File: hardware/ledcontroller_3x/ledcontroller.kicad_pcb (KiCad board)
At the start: 4 copper layers, 35.6 x 59.1 mm, 88 parts, among them J1 ADC, J10 GPIO10, J11 MOSI, J12 SCLK, J13 TX, J14 RX, J15 FLASH, J16 SCL, J17 SDA, J18 OE, J19 Pololu D24V5F3, J2 GPIO16, J20 VIN, J21 GND, J22 24V, J23 RED, J24 GREEN, J25 BLUE, J26 W_WHITE, J27 C_WHITE, J28 24V, J29 RED, J3 GPIO14, J30 GREEN, J31 BLUE, J32 W_WHITE, J33 C_WHITE, J34 24V, J35 RED, J36 GREEN, J37 BLUE, J38 W_WHITE, J39 C_WHITE, J4 GPIO12, J5 GPIO13, J6 RESET, J7 CS0, J8 MISO, J9 GPIO9, Q1 BLM3400, Q10 BLM3400, Q11 BLM3400, Q12 BLM3400, Q13 BLM3400, Q14 BLM3400, Q15 BLM3400, Q2 BLM3400, Q3 BLM3400, Q4 BLM3400, Q5 BLM3400, Q6 BLM3400, Q7 BLM3400, Q8 BLM3400, Q9 BLM3400, U1 ESP-12E, U2 PCA9685PW

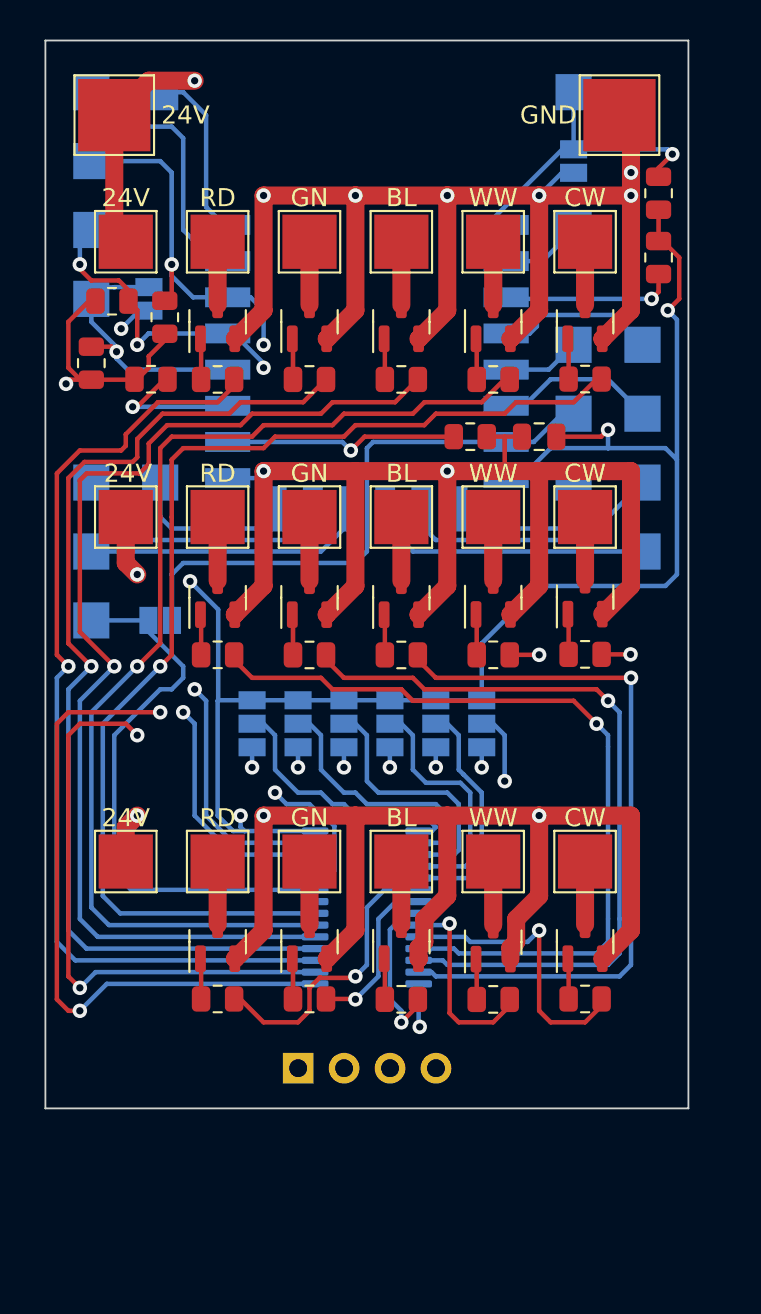
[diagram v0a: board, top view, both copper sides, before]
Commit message: Updated PCB to combat flickering with higher current LEDs or longer strips
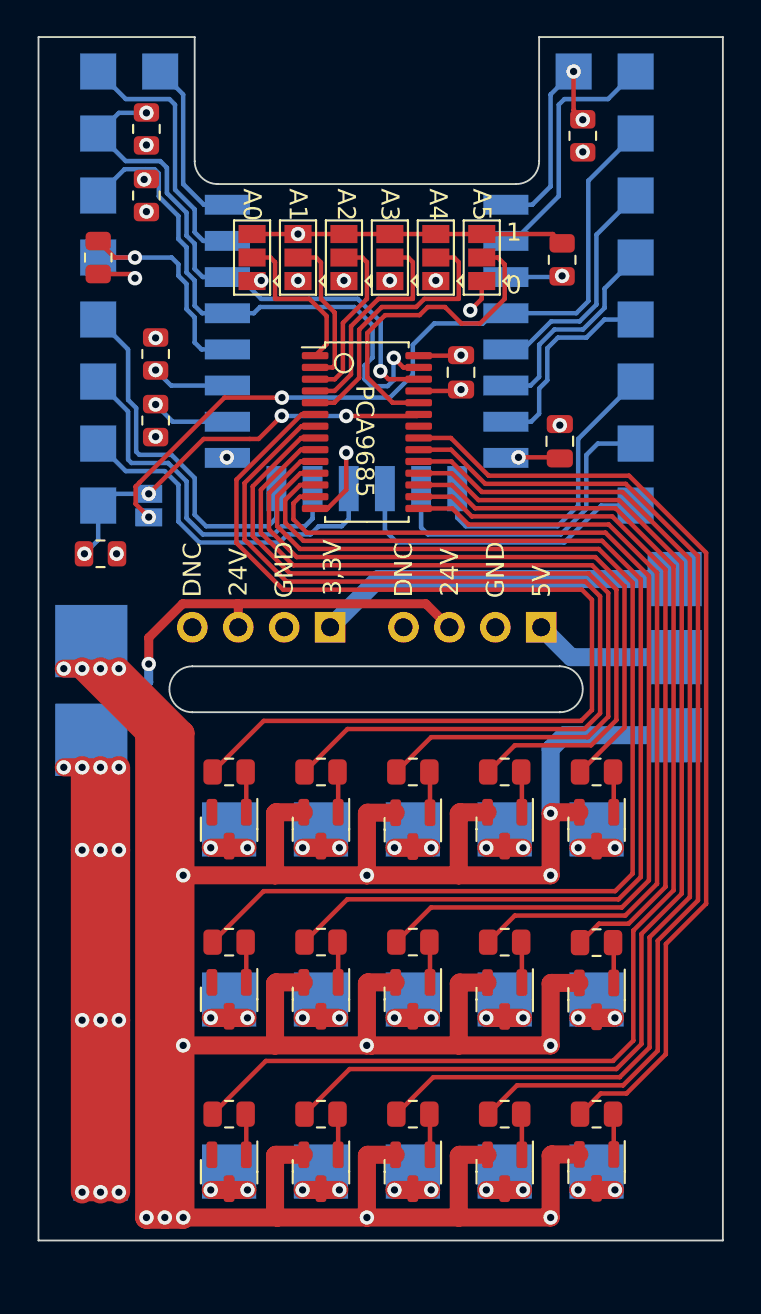
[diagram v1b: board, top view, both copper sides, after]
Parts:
- removed JP8: RESET, Jumper:SolderJumper-2_P1.3mm_Open_Pad1.0x1.5mm
- removed JP9: FLASH, Jumper:SolderJumper-2_P1.3mm_Open_Pad1.0x1.5mm
- added C2: 100nF, Capacitor_SMD:C_0805_2012Metric, F.Cu at (114.8, 68.8)
- added J40: Pololu D24V5F5, Connector_PinHeader_2.54mm:PinHeader_1x04_P2.54mm_Vertical, B.Cu at (113.8, 79.1)
- added J41: AUX, TestPoint:TestPoint_Pad_3.0x3.0mm, B.Cu at (121.2, 80.8)
- added J43: GND, TestPoint:TestPoint_Pad_3.0x3.0mm, B.Cu at (121.2, 85.1)
- added J45: 3.3V, TestPoint:TestPoint_Pad_3.0x3.0mm, B.Cu at (121.2, 76.5)
- added R23: 10k, Resistor_SMD:R_0805_2012Metric, F.Cu at (89.4, 75.1)
- J20, J21, J22, J23, J24, J25, J26, J27, J28, J29, J30, J31, J32, J33, J34, J35, J36, J37, J38, J39: moved to B.Cu
- JP1, JP2, JP3, JP4, JP5, JP7, U2: moved to F.Cu
- moved J22 51.6 mm to (89.4, 109.3), turned to 180 degrees
- moved J23 51.4 mm to (96.5, 109.2), turned to 180 degrees
- moved J24 51.4 mm to (101.6, 109.2), turned to 180 degrees
- moved J25 51.4 mm to (106.7, 109.2), turned to 180 degrees
- moved J26 51.4 mm to (111.8, 109.2), turned to 180 degrees
- moved J27 51.4 mm to (116.8, 109.2), turned to 180 degrees
- moved Q1 47.0 mm to (96.5, 109.2), turned to -90 degrees
- moved Q2 47.0 mm to (101.6, 109.2), turned to -90 degrees
- moved Q3 47.0 mm to (106.7, 109.2), turned to -90 degrees
- moved Q4 47.0 mm to (111.8, 109.2), turned to -90 degrees
- moved Q5 47.0 mm to (116.8, 109.2), turned to -90 degrees
- moved J21 41.2 mm to (88.9, 79.9), turned to 180 degrees
- moved R12 40.7 mm to (116.8, 106.0), turned to 0 degrees
- moved R10 40.6 mm to (106.7, 106.0), turned to 0 degrees
- moved R11 40.6 mm to (111.8, 106.0), turned to 0 degrees
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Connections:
- net Net-(R3-Pad2) renamed /RST
- net Net-(R5-Pad2) renamed /FLS
- net Net-(U1-Pad17) renamed /CS0
- net Net-(U1-Pad18) renamed /MISO
- net Net-(U1-Pad19) renamed /G9
- net Net-(U1-Pad2) renamed /ADC
- net Net-(U1-Pad20) renamed /G10
- net Net-(U1-Pad21) renamed /MOSI
- net Net-(U1-Pad22) renamed /SCLK
- net Net-(U1-Pad5) renamed /G14
- net Net-(U1-Pad6) renamed /G12
- net Net-(U2-Pad1) renamed /A0
- net Net-(U2-Pad2) renamed /A1
- net Net-(U2-Pad23) renamed /OE
- net Net-(U2-Pad24) renamed /A5
- net Net-(U2-Pad3) renamed /A2
- net Net-(U2-Pad4) renamed /A3
- net Net-(U2-Pad5) renamed /A4
- J2 pad 1: Net-(U1-Pad4) -> /G16
- J5 pad 1: Net-(U1-Pad7) -> /G13
- JP6 pad 1: Net-(U1-Pad7) -> /G16
- U1 pad 4: Net-(U1-Pad4) -> /G16
- U1 pad 7: Net-(U1-Pad7) -> /G13
- U2 pad 25: unconnected-(U2-Pad25) -> GND
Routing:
- net +24V: track 18.7 -> 105.8 mm, vias 3 -> 14
- net +3.3V: track 129.1 -> 44.3 mm, vias 5 -> 9
- net /Green0: track 9.23 -> 53.5 mm, vias 1 -> 0
- net /G16: track 0.00 -> 42.6 mm, vias 0 -> 2
- net /Red0: track 16.4 -> 58.8 mm, vias 1 -> 0
- net /Blue0: track 9.00 -> 48.1 mm, vias 1 -> 0
- net Net-(U1-Pad7): track 31.8 -> 0.00 mm
- net /WW0: track 11.0 -> 42.8 mm, vias 1 -> 0
- net GND: track 213.3 -> 241.3 mm, vias 18 -> 27
- net /SCL: track 57.3 -> 30.5 mm, vias 3 -> 2
- net /CW1: track 65.4 -> 38.9 mm, vias 3 -> 0
- net /CW0: track 16.0 -> 37.5 mm, vias 1 -> 0
- net /Red1: track 45.0 -> 66.1 mm, vias 1 -> 0
- net /SDA: track 51.2 -> 31.2 mm, vias 4 -> 2
- net /WW1: track 61.9 -> 42.5 mm, vias 3 -> 0
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- added copper zone on In1.Cu, net +24V
- added copper zone on In1.Cu, net +3.3V
- added copper zone on In2.Cu, net GND
- removed copper zone on In2.Cu, net +24V
- removed copper zone on In1.Cu, net GND
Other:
- board size 35.6 x 59.1 mm -> 37.8 x 66.5 mm
- board text added: "0"
- board text added: "1"
- board text added: "3,3V"
- board text added: "3.3V"
- board text added: "5V"
- board text added: "CH1"
- board text added: "CH2"
- board text added: "CH3"
- board text added: "CS"
- board text added: "DNC"
- board text added: "G9"
- board text added: "INPUT"
- board text added: "OE-G16"
- board text added: "OUTPUT"
- board text removed: "CS0"
- board text removed: "DNC,24V,GND,3.3V"
- board text removed: "G09"

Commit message: Updated PCB: additional decoupling capacitors, switchable I2C pullups, made OE pulled down instead of pulled up
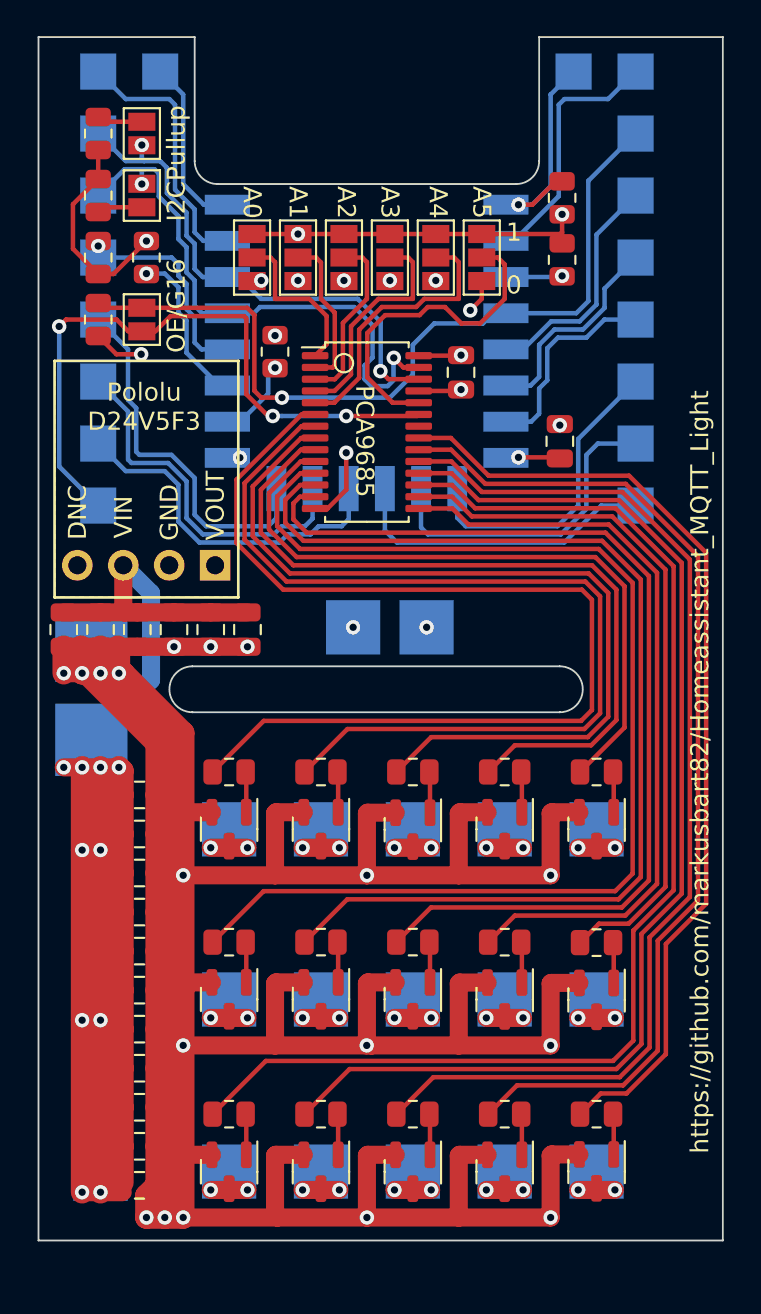
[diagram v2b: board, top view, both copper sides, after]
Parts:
- removed J40: Pololu D24V5F5, Connector_PinHeader_2.54mm:PinHeader_1x04_P2.54mm_Vertical
- removed J41: AUX, TestPoint:TestPoint_Pad_3.0x3.0mm
- added C10: 10uF 50V, Capacitor_SMD:C_0805_2012Metric, F.Cu at (91.6, 94.9)
- added C11: 10uF 50V, Capacitor_SMD:C_0805_2012Metric, F.Cu at (91.6, 92.7)
- added C12: 10uF 50V, Capacitor_SMD:C_0805_2012Metric, F.Cu at (91.6, 90.6)
- added C13: 10uF 50V, Capacitor_SMD:C_0805_2012Metric, F.Cu at (91.6, 88.4)
- added C14: 10uF 50V, Capacitor_SMD:C_0805_2012Metric, F.Cu at (87.4, 79.2)
- added C15: 10uF 50V, Capacitor_SMD:C_0805_2012Metric, F.Cu at (89.4, 79.2)
- added C16: 10uF 50V, Capacitor_SMD:C_0805_2012Metric, F.Cu at (91.4, 79.2)
- added C17: 10uF 50V, Capacitor_SMD:C_0805_2012Metric, F.Cu at (93.5, 79.2)
- added C18: 10uF 50V, Capacitor_SMD:C_0805_2012Metric, F.Cu at (95.5, 79.2)
- added C19: 10uF 50V, Capacitor_SMD:C_0805_2012Metric, F.Cu at (97.5, 79.2)
- added C3: 10uF 50V, Capacitor_SMD:C_0805_2012Metric, F.Cu at (91.6, 110.0)
- added C4: 10uF 50V, Capacitor_SMD:C_0805_2012Metric, F.Cu at (91.6, 107.8)
- added C5: 10uF 50V, Capacitor_SMD:C_0805_2012Metric, F.Cu at (91.6, 105.7)
- added C6: 10uF 50V, Capacitor_SMD:C_0805_2012Metric, F.Cu at (91.6, 103.5)
- added C7: 10uF 50V, Capacitor_SMD:C_0805_2012Metric, F.Cu at (91.6, 101.3)
- added C8: 10uF 50V, Capacitor_SMD:C_0805_2012Metric, F.Cu at (91.6, 99.2)
- added C9: 10uF 50V, Capacitor_SMD:C_0805_2012Metric, F.Cu at (91.6, 97.0)
- added JP8: OE, Jumper:SolderJumper-2_P1.3mm_Open_Pad1.0x1.5mm, F.Cu at (91.7, 51.8)
- added JP9: OE, Jumper:SolderJumper-2_P1.3mm_Open_Pad1.0x1.5mm, F.Cu at (91.7, 55.2)
- JP6: moved to F.Cu
- moved J45 18.0 mm to (103.4, 79.1)
- moved J43 15.0 mm to (107.4, 79.1)
- moved R23 13.0 mm to (89.3, 62.1), turned to 90 degrees
- moved JP6 10.3 mm to (91.7, 62.1), turned to -90 degrees
- moved R7 7.62 mm to (99.1, 63.9), turned to -90 degrees
- moved J19 7.23 mm to (95.7, 75.7)
- moved R6 5.36 mm to (91.9, 58.7)
- moved R3 3.61 mm to (114.9, 55.4)
- moved R1 2.68 mm to (89.3, 51.8)
- moved R2 2.67 mm to (89.3, 55.2), turned to -90 degrees
- moved J21 0.25 mm to (88.9, 80.1)
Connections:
- R1 pad 2: /SCL -> Net-(R1-Pad2)
- R2 pad 2: /SDA -> Net-(R2-Pad2)
- R23 pad 1: /OE -> GND
- R23 pad 2: +3.3V -> /G16
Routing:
- net GND: track 241.3 -> 256.8 mm, vias 27 -> 31
- net /OE: track 22.8 -> 36.2 mm, vias 4 -> 3
- net +3.3V: track 44.3 -> 34.9 mm, vias 9 -> 6
- net +5V: track 8.06 -> 0.00 mm
- net Net-(R6-Pad1): track 5.02 -> 9.60 mm
- net +24V: track 105.8 -> 101.8 mm, vias 14 -> 10
- net /G16: track 42.6 -> 45.3 mm, vias 2 -> 1
- net Net-(R2-Pad2): track 0.00 -> 2.52 mm
- net Net-(R1-Pad2): track 0.00 -> 2.52 mm
- net /FLS: track 14.4 -> 12.0 mm
- net /SCL: track 30.5 -> 28.3 mm
- net Net-(R7-Pad2): track 5.06 -> 3.78 mm
- net /RST: track 13.3 -> 13.4 mm, vias 2 -> 1
- added copper zone on F.Cu, net GND
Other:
- board text added: "I2CPullup"
- board text added: "IN"
- board text added: "OE/G16"
- board text added: "OUT"
- board text added: "Pololu D24V5F3"
- board text added: "VIN"
- board text added: "VOUT"
- board text added: "https://github.com/markusbart82/Homeassistant_MQTT_Light"
- board text removed: "3,3V"
- board text removed: "5V"
- board text removed: "INPUT"
- board text removed: "OE-G16"
- board text removed: "OUTPUT"

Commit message: replaced ceramic capacitors with low ESR electrolytic caps
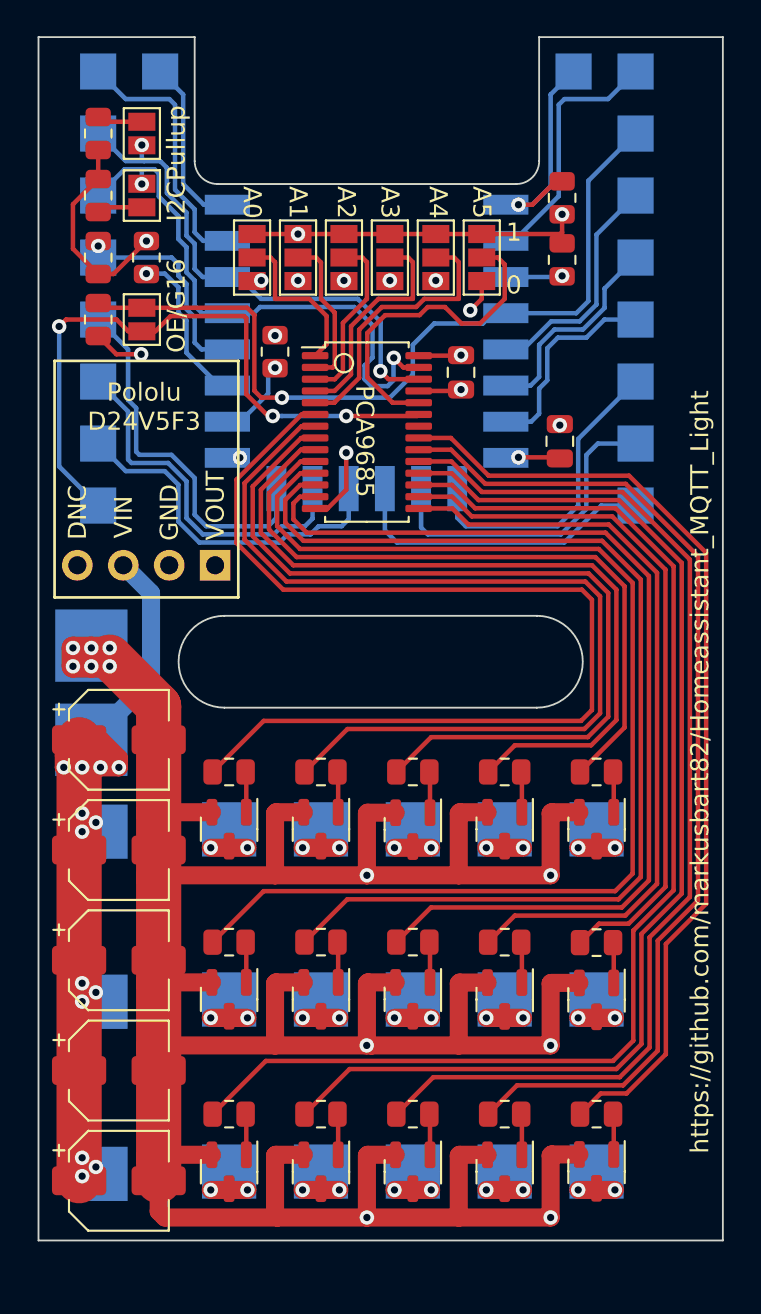
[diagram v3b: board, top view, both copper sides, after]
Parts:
- removed C10, C11, C12, C13, C14, C15, C16, C17, C18, C19, C8, C9: 10uF 50V, Capacitor_SMD:C_0805_2012Metric
- removed J43: GND, TestPoint:TestPoint_Pad_3.0x3.0mm
- removed J45: 3.3V, TestPoint:TestPoint_Pad_3.0x3.0mm
- C3, C4, C5, C6, C7: value 10uF 50V -> 10uF; footprint Capacitor_SMD:C_0805_2012Metric -> Capacitor_SMD:CP_Elec_5x5.4
- moved C3 24.7 mm to (90.4, 85.3)
- moved C4 16.4 mm to (90.4, 91.4)
- moved C7 8.46 mm to (90.4, 109.7)
- moved C5 8.21 mm to (90.4, 97.5)
- moved C6 1.15 mm to (90.4, 103.6)
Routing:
- net GND: track 256.8 -> 184.0 mm, vias 31 -> 24
- net +24V: track 101.8 -> 47.7 mm, vias 10 -> 13
- net +3.3V: vias 6 -> 5
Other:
- outline, holes or cut-outs redrawn
- board text removed: "3.3V"
- board text removed: "OUT"

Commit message: Added PCB Edge Connector for programming, rearranged lots of parts, removed pads of unused GPIOs
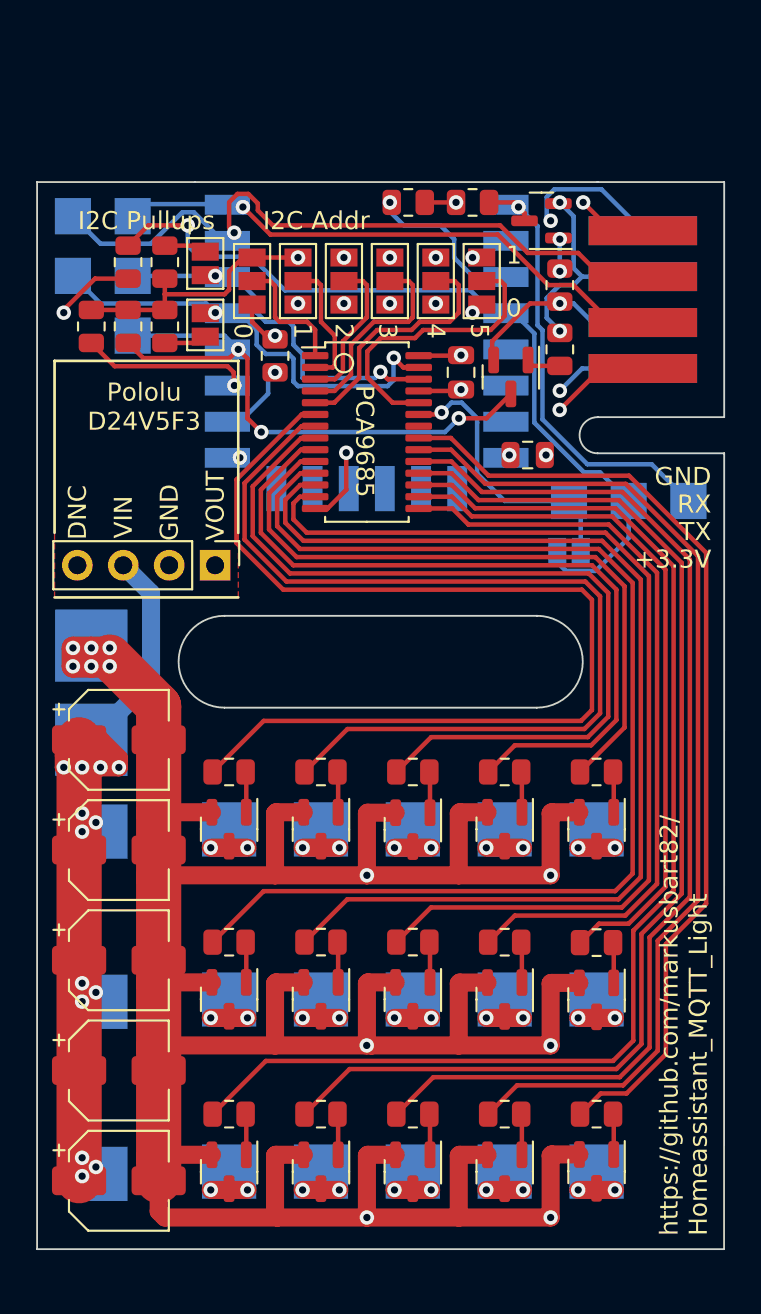
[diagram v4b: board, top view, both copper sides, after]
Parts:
- removed J1: ADC, TestPoint:TestPoint_Pad_2.0x2.0mm
- removed J10: GPIO10, TestPoint:TestPoint_Pad_2.0x2.0mm
- removed J11: MOSI, TestPoint:TestPoint_Pad_2.0x2.0mm
- removed J12: SCLK, TestPoint:TestPoint_Pad_2.0x2.0mm
- removed J3: GPIO14, TestPoint:TestPoint_Pad_2.0x2.0mm
- removed J4: GPIO12, TestPoint:TestPoint_Pad_2.0x2.0mm
- removed J5: GPIO13, TestPoint:TestPoint_Pad_2.0x2.0mm
- removed J7: CS0, TestPoint:TestPoint_Pad_2.0x2.0mm
- removed J8: MISO, TestPoint:TestPoint_Pad_2.0x2.0mm
- removed J9: GPIO9, TestPoint:TestPoint_Pad_2.0x2.0mm
- added J41: Flash Adapter, Connector_Card_Edge:WingTAT_ED08BGFBK, F.Cu at (121.9, 61.0)
- added Q16: MMS9013-H-TP, Package_TO_SOT_SMD:SOT-23, F.Cu at (113.8, 56.6)
- added Q17: MMS9013-H-TP, Package_TO_SOT_SMD:SOT-23, F.Cu at (112.1, 65.3)
- added R24: 10k, Resistor_SMD:R_0805_2012Metric, F.Cu at (114.8, 60.2)
- added R25: 10k, Resistor_SMD:R_0805_2012Metric, F.Cu at (114.8, 63.8)
- C3, C4, C5, C6, C7: value 10uF -> 10uF 35V
- J19: moved to F.Cu
- JP6: moved to B.Cu
- moved JP6 26.9 mm to (115.3, 74.9), turned to 0 degrees
- moved J18 26.0 mm to (115.3, 72.1)
- moved J6 24.6 mm to (121.9, 72.1)
- moved J2 20.3 mm to (118.6, 72.1)
- moved R4 9.08 mm to (106.4, 55.6), turned to 180 degrees
- moved J13 8.14 mm to (91.2, 56.4)
- moved R2 8.12 mm to (93.0, 62.5)
- moved J14 8.12 mm to (87.9, 56.4)
- moved J16 8.10 mm to (91.2, 59.7)
- moved R1 8.01 mm to (93.0, 58.9)
- moved JP8 7.99 mm to (95.2, 59.0)
- moved JP9 7.97 mm to (95.2, 62.4)
- moved R3 4.96 mm to (110.0, 55.6), turned to 0 degrees
- moved R6 4.88 mm to (88.9, 62.5)
- moved J15 4.72 mm to (91.2, 63.0)
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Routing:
- net /RX: track 15.2 -> 38.8 mm, vias 0 -> 1
- net /TX: track 10.4 -> 31.8 mm, vias 0 -> 1
- net /SCLK: track 21.3 -> 0.00 mm
- net /MOSI: track 20.8 -> 0.00 mm
- net /FLS: track 12.0 -> 32.6 mm, vias 1 -> 3
- net /OE: track 36.2 -> 15.7 mm, vias 3 -> 1
- net /G10: track 20.2 -> 0.00 mm
- net /MISO: track 18.7 -> 0.00 mm
- net /G9: track 18.0 -> 0.00 mm
- net /CS0: track 17.8 -> 0.00 mm
- net /ADC: track 14.7 -> 0.00 mm
- net /G14: track 13.7 -> 0.00 mm
- net /RTS: track 0.00 -> 12.5 mm, vias 0 -> 2
- net /G12: track 12.5 -> 0.00 mm
- net /G13: track 12.1 -> 0.00 mm
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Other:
- board size 37.8 x 66.5 mm -> 38 x 59 mm
- board text added: "+3.3V"
- board text added: "2"
- board text added: "3"
- board text added: "4"
- board text added: "5"
- board text added: "DRT"
- board text added: "I2C Addr"
- board text added: "I2C Pullups"
- board text added: "RTS"
- board text added: "https://github.com/markusbart82/ Homeassistant_MQTT_Light"
- board text removed: "A0"
- board text removed: "A1"
- board text removed: "A2"
- board text removed: "A3"
- board text removed: "A4"
- board text removed: "A5"
- board text removed: "ADC"
- board text removed: "CS"
- board text removed: "G10"
- board text removed: "G12"
- board text removed: "G13"
- board text removed: "G14"
- board text removed: "G9"
- board text removed: "I2CPullup"
- board text removed: "MISO"
- board text removed: "MOSI"
- board text removed: "OE/G16"
- board text removed: "SCLK"
- board text removed: "https://github.com/markusbart82/Homeassistant_MQTT_Light"
